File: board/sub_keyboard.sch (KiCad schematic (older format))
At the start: 48 parts

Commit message: Updated keyboard
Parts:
- removed D? (x23): D, symbol Device:D
- removed SW? (x23): SW_SPST, symbol Switch:SW_SPST
- added D802, D803, D804, D805, D806, D807, D808, D809, D810, D811, D812, D813, D814, D815, D816, D817, D818, D819, D820, D821, D822, D823, D824, D825, D826, D827, D828, D829, D830: D, symbol Device:D
- added SW802, SW803, SW804, SW805, SW806, SW807, SW808, SW809, SW810, SW811, SW812, SW813, SW814, SW815, SW816, SW817, SW818, SW819, SW820, SW821, SW822, SW823, SW824, SW825, SW826, SW827, SW828, SW829, SW830: SW_SPST, symbol Switch:SW_SPST
- gave numbers to parts that had none: 2
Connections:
- net labels added: column[0], column[1], column[2], column[3], column[4], column[5], row[0], row[1], row[2], row[3], row[4]
- wire segments 0 -> 120
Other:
- moved on the sheet: SW801

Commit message: More progress on the schematic. 6502 Done.
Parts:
- renumbered D801 to D701, D802 to D702, D803 to D703, D804 to D704, D805 to D705, D806 to D706, D807 to D707, D808 to D708, D809 to D709, D810 to D710, D811 to D711, D812 to D712, D813 to D713, D814 to D714, D815 to D715, D816 to D716, D817 to D717, D818 to D718, D819 to D719, D820 to D720, D821 to D721, D822 to D722, D823 to D723, D824 to D724, D825 to D725, D826 to D726, D827 to D727, D828 to D728, D829 to D729, D830 to D730, SW801 to SW701, SW802 to SW702, SW803 to SW703, SW804 to SW704, SW805 to SW705, SW806 to SW706, SW807 to SW707, SW808 to SW708, SW809 to SW709, SW810 to SW710, SW811 to SW711, SW812 to SW712, SW813 to SW713, SW814 to SW714, SW815 to SW715, SW816 to SW716, SW817 to SW717, SW818 to SW718, SW819 to SW719, SW820 to SW720, SW821 to SW721, SW822 to SW722, SW823 to SW723, SW824 to SW724, SW825 to SW725, SW826 to SW726, SW827 to SW727, SW828 to SW728, SW829 to SW729, SW830 to SW730

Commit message: Level converters complete, display almost done
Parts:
- removed D701, D702, D703, D704, D705, D706, D707, D708, D709, D710, D711, D712, D713, D714, D715, D716, D717, D718, D719, D720, D721, D722, D723, D724, D725, D726, D727, D728, D729, D730: D, symbol Device:D
- renumbered SW701 to SW1001, SW702 to SW1002, SW703 to SW1003, SW704 to SW1004, SW705 to SW1005, SW706 to SW1006, SW707 to SW1007, SW708 to SW1008, SW709 to SW1009, SW710 to SW1010, SW711 to SW1011, SW712 to SW1012, SW713 to SW1013, SW714 to SW1014, SW715 to SW1015, SW716 to SW1016, SW717 to SW1017, SW718 to SW1018, SW719 to SW1019, SW720 to SW1020, SW721 to SW1021, SW722 to SW1022, SW723 to SW1023, SW724 to SW1024, SW725 to SW1025, SW726 to SW1026, SW727 to SW1027, SW728 to SW1028, SW729 to SW1029, SW730 to SW1030

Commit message: More Schematic progress
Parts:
- renumbered SW1001 to SW901, SW1002 to SW902, SW1003 to SW903, SW1004 to SW904, SW1005 to SW905, SW1006 to SW906, SW1007 to SW907, SW1008 to SW908, SW1009 to SW909, SW1010 to SW910, SW1011 to SW911, SW1012 to SW912, SW1013 to SW913, SW1014 to SW914, SW1015 to SW915, SW1016 to SW916, SW1017 to SW917, SW1018 to SW918, SW1019 to SW919, SW1020 to SW920, SW1021 to SW921, SW1022 to SW922, SW1023 to SW923, SW1024 to SW924, SW1025 to SW925, SW1026 to SW926, SW1027 to SW927, SW1028 to SW928, SW1029 to SW929, SW1030 to SW930
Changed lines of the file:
@@
 $Descr A4 11693 8268
 encoding utf-8
-Sheet 10 15
+Sheet 9 14
 Title ""
 Date ""
@@
 row[4:0]
 $Comp
-L Switch:SW_SPST SW1001
+L Switch:SW_SPST SW901
 U 1 1 5A9DE7BF
 P 4600 2500
-F 0 "SW1001" H 4500 2450 50  0000 L CNN
+F 0 "SW901" H 4500 2450 50  0000 L CNN
 F 1 "SW_SPST" H 4450 2350 50  0001 L CNN
 F 2 "" H 4600 2500 50  0001 C CNN
@@
 $EndComp
 $Comp
-L Switch:SW_SPST SW1006
+L Switch:SW_SPST SW906
 U 1 1 5A9F6D51
 P 5250 2500
-F 0 "SW1006" H 5150 2450 50  0000 L CNN
+F 0 "SW906" H 5150 2450 50  0000 L CNN
 F 1 "SW_SPST" H 5100 2350 50  0001 L CNN
 F 2 "" H 5250 2500 50  0001 C CNN
@@
 $EndComp
 $Comp
-L Switch:SW_SPST SW1011
+L Switch:SW_SPST SW911
 U 1 1 5A9F724F
 P 5900 2500
-F 0 "SW1011" H 5800 2450 50  0000 L CNN
+F 0 "SW911" H 5800 2450 50  0000 L CNN
 F 1 "SW_SPST" H 5750 2350 50  0001 L CNN
 F 2 "" H 5900 2500 50  0001 C CNN
@@
 $EndComp
 $Comp
-L Switch:SW_SPST SW1016
+L Switch:SW_SPST SW916
 U 1 1 5A9F725B
 P 6550 2500
-F 0 "SW1016" H 6450 2450 50  0000 L CNN
+F 0 "SW916" H 6450 2450 50  0000 L CNN
 F 1 "SW_SPST" H 6400 2350 50  0001 L CNN
 F 2 "" H 6550 2500 50  0001 C CNN
@@
 $EndComp
 $Comp
-L Switch:SW_SPST SW1021
+L Switch:SW_SPST SW921
 U 1 1 5A9F738F
 P 7200 2500
-F 0 "SW1021" H 7100 2450 50  0000 L CNN
+F 0 "SW921" H 7100 2450 50  0000 L CNN
 F 1 "SW_SPST" H 7050 2350 50  0001 L CNN
 F 2 "" H 7200 2500 50  0001 C CNN
@@
 $EndComp
 $Comp
-L Switch:SW_SPST SW1026
+L Switch:SW_SPST SW926
 U 1 1 5A9F739B
 P 7850 2500
-F 0 "SW1026" H 7750 2450 50  0000 L CNN
+F 0 "SW926" H 7750 2450 50  0000 L CNN
 F 1 "SW_SPST" H 7700 2350 50  0001 L CNN
 F 2 "" H 7850 2500 50  0001 C CNN
@@
 $EndComp
 $Comp
-L Switch:SW_SPST SW1002
+L Switch:SW_SPST SW902
 U 1 1 5A9F7527
 P 4600 3050
-F 0 "SW1002" H 4500 3000 50  0000 L CNN
+F 0 "SW902" H 4500 3000 50  0000 L CNN
 F 1 "SW_SPST" H 4450 2900 50  0001 L CNN
 F 2 "" H 4600 3050 50  0001 C CNN
@@
 $EndComp
 $Comp
-L Switch:SW_SPST SW1007
+L Switch:SW_SPST SW907
 U 1 1 5A9F7533
 P 5250 3050
-F 0 "SW1007" H 5150 3000 50  0000 L CNN
+F 0 "SW907" H 5150 3000 50  0000 L CNN
 F 1 "SW_SPST" H 5100 2900 50  0001 L CNN
 F 2 "" H 5250 3050 50  0001 C CNN
@@
 $EndComp
 $Comp
-L Switch:SW_SPST SW1012
+L Switch:SW_SPST SW912
 U 1 1 5A9F753F
 P 5900 3050
-F 0 "SW1012" H 5800 3000 50  0000 L CNN
+F 0 "SW912" H 5800 3000 50  0000 L CNN
 F 1 "SW_SPST" H 5750 2900 50  0001 L CNN
 F 2 "" H 5900 3050 50  0001 C CNN
@@
 $EndComp
 $Comp
-L Switch:SW_SPST SW1017
+L Switch:SW_SPST SW917
 U 1 1 5A9F754B
 P 6550 3050
-F 0 "SW1017" H 6450 3000 50  0000 L CNN
+F 0 "SW917" H 6450 3000 50  0000 L CNN
 F 1 "SW_SPST" H 6400 2900 50  0001 L CNN
 F 2 "" H 6550 3050 50  0001 C CNN
@@
 $EndComp
 $Comp
-L Switch:SW_SPST SW1022
+L Switch:SW_SPST SW922
 U 1 1 5A9F7557
 P 7200 3050
-F 0 "SW1022" H 7100 3000 50  0000 L CNN
+F 0 "SW922" H 7100 3000 50  0000 L CNN
 F 1 "SW_SPST" H 7050 2900 50  0001 L CNN
 F 2 "" H 7200 3050 50  0001 C CNN
@@
 $EndComp
 $Comp
-L Switch:SW_SPST SW1027
+L Switch:SW_SPST SW927
 U 1 1 5A9F7563
 P 7850 3050
-F 0 "SW1027" H 7750 3000 50  0000 L CNN
+F 0 "SW927" H 7750 3000 50  0000 L CNN
 F 1 "SW_SPST" H 7700 2900 50  0001 L CNN
 F 2 "" H 7850 3050 50  0001 C CNN
@@
 $EndComp
 $Comp
-L Switch:SW_SPST SW1003
+L Switch:SW_SPST SW903
 U 1 1 5A9F8C97
 P 4600 3600
-F 0 "SW1003" H 4500 3550 50  0000 L CNN
+F 0 "SW903" H 4500 3550 50  0000 L CNN
 F 1 "SW_SPST" H 4450 3450 50  0001 L CNN
 F 2 "" H 4600 3600 50  0001 C CNN
@@
 $EndComp
 $Comp
-L Switch:SW_SPST SW1008
+L Switch:SW_SPST SW908
 U 1 1 5A9F8CA3
 P 5250 3600
-F 0 "SW1008" H 5150 3550 50  0000 L CNN
+F 0 "SW908" H 5150 3550 50  0000 L CNN
 F 1 "SW_SPST" H 5100 3450 50  0001 L CNN
 F 2 "" H 5250 3600 50  0001 C CNN
@@
 $EndComp
 $Comp
-L Switch:SW_SPST SW1013
+L Switch:SW_SPST SW913
 U 1 1 5A9F8CAF
 P 5900 3600
-F 0 "SW1013" H 5800 3550 50  0000 L CNN
+F 0 "SW913" H 5800 3550 50  0000 L CNN
 F 1 "SW_SPST" H 5750 3450 50  0001 L CNN
 F 2 "" H 5900 3600 50  0001 C CNN
@@
 $EndComp
 $Comp
-L Switch:SW_SPST SW1018
+L Switch:SW_SPST SW918
 U 1 1 5A9F8CBB
 P 6550 3600
-F 0 "SW1018" H 6450 3550 50  0000 L CNN
+F 0 "SW918" H 6450 3550 50  0000 L CNN
 F 1 "SW_SPST" H 6400 3450 50  0001 L CNN
 F 2 "" H 6550 3600 50  0001 C CNN
@@
 $EndComp
 $Comp
-L Switch:SW_SPST SW1023
+L Switch:SW_SPST SW923
 U 1 1 5A9F8CC7
 P 7200 3600
-F 0 "SW1023" H 7100 3550 50  0000 L CNN
+F 0 "SW923" H 7100 3550 50  0000 L CNN
 F 1 "SW_SPST" H 7050 3450 50  0001 L CNN
 F 2 "" H 7200 3600 50  0001 C CNN
@@
 $EndComp
 $Comp
-L Switch:SW_SPST SW1028
+L Switch:SW_SPST SW928
 U 1 1 5A9F8CD3
 P 7850 3600
-F 0 "SW1028" H 7750 3550 50  0000 L CNN
+F 0 "SW928" H 7750 3550 50  0000 L CNN
 F 1 "SW_SPST" H 7700 3450 50  0001 L CNN
 F 2 "" H 7850 3600 50  0001 C CNN
@@
 $EndComp
 $Comp
-L Switch:SW_SPST SW1004
+L Switch:SW_SPST SW904
 U 1 1 5A9F94D7
 P 4600 4150
-F 0 "SW1004" H 4500 4100 50  0000 L CNN
+F 0 "SW904" H 4500 4100 50  0000 L CNN
 F 1 "SW_SPST" H 4450 4000 50  0001 L CNN
 F 2 "" H 4600 4150 50  0001 C CNN
@@
 $EndComp
 $Comp
-L Switch:SW_SPST SW1009
+L Switch:SW_SPST SW909
 U 1 1 5A9F94E3
 P 5250 4150
-F 0 "SW1009" H 5150 4100 50  0000 L CNN
+F 0 "SW909" H 5150 4100 50  0000 L CNN
 F 1 "SW_SPST" H 5100 4000 50  0001 L CNN
 F 2 "" H 5250 4150 50  0001 C CNN
@@
 $EndComp
 $Comp
-L Switch:SW_SPST SW1014
+L Switch:SW_SPST SW914
 U 1 1 5A9F94EF
 P 5900 4150
-F 0 "SW1014" H 5800 4100 50  0000 L CNN
+F 0 "SW914" H 5800 4100 50  0000 L CNN
 F 1 "SW_SPST" H 5750 4000 50  0001 L CNN
 F 2 "" H 5900 4150 50  0001 C CNN
@@
 $EndComp
 $Comp
-L Switch:SW_SPST SW1019
+L Switch:SW_SPST SW919
 U 1 1 5A9F94FB
 P 6550 4150
-F 0 "SW1019" H 6450 4100 50  0000 L CNN
+F 0 "SW919" H 6450 4100 50  0000 L CNN
 F 1 "SW_SPST" H 6400 4000 50  0001 L CNN
 F 2 "" H 6550 4150 50  0001 C CNN
@@
 $EndComp
 $Comp
-L Switch:SW_SPST SW1024
+L Switch:SW_SPST SW924
 U 1 1 5A9F9507
 P 7200 4150
-F 0 "SW1024" H 7100 4100 50  0000 L CNN
+F 0 "SW924" H 7100 4100 50  0000 L CNN
 F 1 "SW_SPST" H 7050 4000 50  0001 L CNN
 F 2 "" H 7200 4150 50  0001 C CNN
@@
 $EndComp
 $Comp
-L Switch:SW_SPST SW1029
+L Switch:SW_SPST SW929
 U 1 1 5A9F9513
 P 7850 4150
-F 0 "SW1029" H 7750 4100 50  0000 L CNN
+F 0 "SW929" H 7750 4100 50  0000 L CNN
 F 1 "SW_SPST" H 7700 4000 50  0001 L CNN
 F 2 "" H 7850 4150 50  0001 C CNN
@@
 $EndComp
 $Comp
-L Switch:SW_SPST SW1005
+L Switch:SW_SPST SW905
 U 1 1 5A9F951F
 P 4600 4700
-F 0 "SW1005" H 4500 4650 50  0000 L CNN
+F 0 "SW905" H 4500 4650 50  0000 L CNN
 F 1 "SW_SPST" H 4450 4550 50  0001 L CNN
 F 2 "" H 4600 4700 50  0001 C CNN
@@
 $EndComp
 $Comp
-L Switch:SW_SPST SW1010
+L Switch:SW_SPST SW910
 U 1 1 5A9F952B
 P 5250 4700
-F 0 "SW1010" H 5150 4650 50  0000 L CNN
+F 0 "SW910" H 5150 4650 50  0000 L CNN
 F 1 "SW_SPST" H 5100 4550 50  0001 L CNN
 F 2 "" H 5250 4700 50  0001 C CNN
@@
 $EndComp
 $Comp
-L Switch:SW_SPST SW1015
+L Switch:SW_SPST SW915
 U 1 1 5A9F9537
 P 5900 4700
-F 0 "SW1015" H 5800 4650 50  0000 L CNN
+F 0 "SW915" H 5800 4650 50  0000 L CNN
 F 1 "SW_SPST" H 5750 4550 50  0001 L CNN
 F 2 "" H 5900 4700 50  0001 C CNN
@@
 $EndComp
 $Comp
-L Switch:SW_SPST SW1020
+L Switch:SW_SPST SW920
 U 1 1 5A9F9543
 P 6550 4700
-F 0 "SW1020" H 6450 4650 50  0000 L CNN
+F 0 "SW920" H 6450 4650 50  0000 L CNN
 F 1 "SW_SPST" H 6400 4550 50  0001 L CNN
 F 2 "" H 6550 4700 50  0001 C CNN
@@
 $EndComp
 $Comp
-L Switch:SW_SPST SW1025
+L Switch:SW_SPST SW925
 U 1 1 5A9F954F
 P 7200 4700
-F 0 "SW1025" H 7100 4650 50  0000 L CNN
+F 0 "SW925" H 7100 4650 50  0000 L CNN
 F 1 "SW_SPST" H 7050 4550 50  0001 L CNN
 F 2 "" H 7200 4700 50  0001 C CNN
@@
 $EndComp
 $Comp
-L Switch:SW_SPST SW1030
+L Switch:SW_SPST SW930
 U 1 1 5A9F955B
 P 7850 4700
-F 0 "SW1030" H 7750 4650 50  0000 L CNN
+F 0 "SW930" H 7750 4650 50  0000 L CNN
 F 1 "SW_SPST" H 7700 4550 50  0001 L CNN
 F 2 "" H 7850 4700 50  0001 C CNN

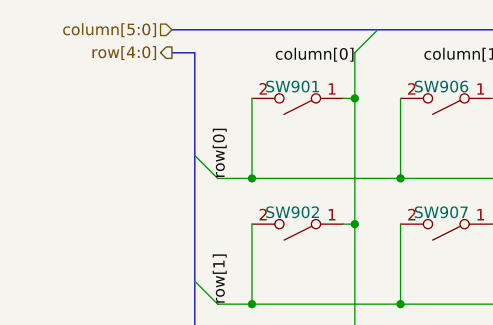
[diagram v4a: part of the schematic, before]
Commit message: Bus signal connectivity rebuilt
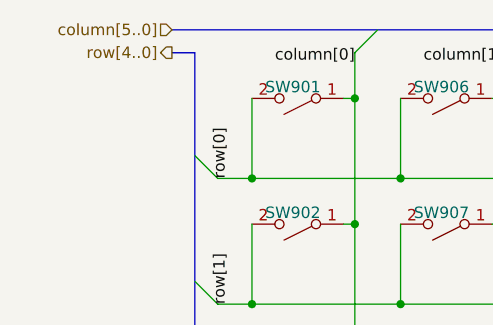
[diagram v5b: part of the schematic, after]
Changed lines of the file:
@@
 $EndDescr
 Text HLabel 4050 2200 0    50   Input ~ 0
-column[5:0]
+column[5..0]
 Text HLabel 4050 2300 0    50   Output ~ 0
-row[4:0]
+row[4..0]
 $Comp
 L Switch:SW_SPST SW901

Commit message: Schematics mostly complete
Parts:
- renumbered SW906 to SW902, SW911 to SW903, SW916 to SW904, SW921 to SW905, SW926 to SW906, SW902 to SW907, SW907 to SW908, SW912 to SW909, SW917 to SW910, SW922 to SW911, SW927 to SW912, SW903 to SW913, SW908 to SW914, SW913 to SW915, SW918 to SW916, SW923 to SW917, SW928 to SW918, SW904 to SW919, SW909 to SW920, SW914 to SW921, SW919 to SW922, SW924 to SW923, SW929 to SW924, SW905 to SW925, SW910 to SW926, SW915 to SW927, SW920 to SW928, SW925 to SW929
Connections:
- net column[0] renamed column0
- net column[1] renamed column1
- net column[2] renamed column2
- net column[3] renamed column3
- net column[4] renamed column4
- net column[5] renamed column5
- net row[0] renamed row0
- net row[1] renamed row1
- net row[2] renamed row2
- net row[3] renamed row3
- net row[4] renamed row4
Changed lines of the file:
@@
 $EndComp
 $Comp
-L Switch:SW_SPST SW906
+L Switch:SW_SPST SW902
 U 1 1 5A9F6D51
 P 5250 2500
-F 0 "SW906" H 5150 2450 50  0000 L CNN
+F 0 "SW902" H 5150 2450 50  0000 L CNN
 F 1 "SW_SPST" H 5100 2350 50  0001 L CNN
 F 2 "" H 5250 2500 50  0001 C CNN
@@
 $EndComp
 $Comp
-L Switch:SW_SPST SW911
+L Switch:SW_SPST SW903
 U 1 1 5A9F724F
 P 5900 2500
-F 0 "SW911" H 5800 2450 50  0000 L CNN
+F 0 "SW903" H 5800 2450 50  0000 L CNN
 F 1 "SW_SPST" H 5750 2350 50  0001 L CNN
 F 2 "" H 5900 2500 50  0001 C CNN
@@
 $EndComp
 $Comp
-L Switch:SW_SPST SW916
+L Switch:SW_SPST SW904
 U 1 1 5A9F725B
 P 6550 2500
-F 0 "SW916" H 6450 2450 50  0000 L CNN
+F 0 "SW904" H 6450 2450 50  0000 L CNN
 F 1 "SW_SPST" H 6400 2350 50  0001 L CNN
 F 2 "" H 6550 2500 50  0001 C CNN
@@
 $EndComp
 $Comp
-L Switch:SW_SPST SW921
+L Switch:SW_SPST SW905
 U 1 1 5A9F738F
 P 7200 2500
-F 0 "SW921" H 7100 2450 50  0000 L CNN
+F 0 "SW905" H 7100 2450 50  0000 L CNN
 F 1 "SW_SPST" H 7050 2350 50  0001 L CNN
 F 2 "" H 7200 2500 50  0001 C CNN
@@
 $EndComp
 $Comp
-L Switch:SW_SPST SW926
+L Switch:SW_SPST SW906
 U 1 1 5A9F739B
 P 7850 2500
-F 0 "SW926" H 7750 2450 50  0000 L CNN
+F 0 "SW906" H 7750 2450 50  0000 L CNN
 F 1 "SW_SPST" H 7700 2350 50  0001 L CNN
 F 2 "" H 7850 2500 50  0001 C CNN
@@
 $EndComp
 $Comp
-L Switch:SW_SPST SW902
+L Switch:SW_SPST SW907
 U 1 1 5A9F7527
 P 4600 3050
-F 0 "SW902" H 4500 3000 50  0000 L CNN
+F 0 "SW907" H 4500 3000 50  0000 L CNN
 F 1 "SW_SPST" H 4450 2900 50  0001 L CNN
 F 2 "" H 4600 3050 50  0001 C CNN
@@
 $EndComp
 $Comp
-L Switch:SW_SPST SW907
+L Switch:SW_SPST SW908
 U 1 1 5A9F7533
 P 5250 3050
-F 0 "SW907" H 5150 3000 50  0000 L CNN
+F 0 "SW908" H 5150 3000 50  0000 L CNN
 F 1 "SW_SPST" H 5100 2900 50  0001 L CNN
 F 2 "" H 5250 3050 50  0001 C CNN
@@
 $EndComp
 $Comp
-L Switch:SW_SPST SW912
+L Switch:SW_SPST SW909
 U 1 1 5A9F753F
 P 5900 3050
-F 0 "SW912" H 5800 3000 50  0000 L CNN
+F 0 "SW909" H 5800 3000 50  0000 L CNN
 F 1 "SW_SPST" H 5750 2900 50  0001 L CNN
 F 2 "" H 5900 3050 50  0001 C CNN
@@
 $EndComp
 $Comp
-L Switch:SW_SPST SW917
+L Switch:SW_SPST SW910
 U 1 1 5A9F754B
 P 6550 3050
-F 0 "SW917" H 6450 3000 50  0000 L CNN
+F 0 "SW910" H 6450 3000 50  0000 L CNN
 F 1 "SW_SPST" H 6400 2900 50  0001 L CNN
 F 2 "" H 6550 3050 50  0001 C CNN
@@
 $EndComp
 $Comp
-L Switch:SW_SPST SW922
+L Switch:SW_SPST SW911
 U 1 1 5A9F7557
 P 7200 3050
-F 0 "SW922" H 7100 3000 50  0000 L CNN
+F 0 "SW911" H 7100 3000 50  0000 L CNN
 F 1 "SW_SPST" H 7050 2900 50  0001 L CNN
 F 2 "" H 7200 3050 50  0001 C CNN
@@
 $EndComp
 $Comp
-L Switch:SW_SPST SW927
+L Switch:SW_SPST SW912
 U 1 1 5A9F7563
 P 7850 3050
-F 0 "SW927" H 7750 3000 50  0000 L CNN
+F 0 "SW912" H 7750 3000 50  0000 L CNN
 F 1 "SW_SPST" H 7700 2900 50  0001 L CNN
 F 2 "" H 7850 3050 50  0001 C CNN
@@
 $EndComp
 $Comp
-L Switch:SW_SPST SW903
+L Switch:SW_SPST SW913
 U 1 1 5A9F8C97
 P 4600 3600
-F 0 "SW903" H 4500 3550 50  0000 L CNN
+F 0 "SW913" H 4500 3550 50  0000 L CNN
 F 1 "SW_SPST" H 4450 3450 50  0001 L CNN
 F 2 "" H 4600 3600 50  0001 C CNN
@@
 $EndComp
 $Comp
-L Switch:SW_SPST SW908
+L Switch:SW_SPST SW914
 U 1 1 5A9F8CA3
 P 5250 3600
-F 0 "SW908" H 5150 3550 50  0000 L CNN
+F 0 "SW914" H 5150 3550 50  0000 L CNN
 F 1 "SW_SPST" H 5100 3450 50  0001 L CNN
 F 2 "" H 5250 3600 50  0001 C CNN
@@
 $EndComp
 $Comp
-L Switch:SW_SPST SW913
+L Switch:SW_SPST SW915
 U 1 1 5A9F8CAF
 P 5900 3600
-F 0 "SW913" H 5800 3550 50  0000 L CNN
+F 0 "SW915" H 5800 3550 50  0000 L CNN
 F 1 "SW_SPST" H 5750 3450 50  0001 L CNN
 F 2 "" H 5900 3600 50  0001 C CNN
@@
 $EndComp
 $Comp
-L Switch:SW_SPST SW918
+L Switch:SW_SPST SW916
 U 1 1 5A9F8CBB
 P 6550 3600
-F 0 "SW918" H 6450 3550 50  0000 L CNN
+F 0 "SW916" H 6450 3550 50  0000 L CNN
 F 1 "SW_SPST" H 6400 3450 50  0001 L CNN
 F 2 "" H 6550 3600 50  0001 C CNN
@@
 $EndComp
 $Comp
-L Switch:SW_SPST SW923
+L Switch:SW_SPST SW917
 U 1 1 5A9F8CC7
 P 7200 3600
-F 0 "SW923" H 7100 3550 50  0000 L CNN
+F 0 "SW917" H 7100 3550 50  0000 L CNN
 F 1 "SW_SPST" H 7050 3450 50  0001 L CNN
 F 2 "" H 7200 3600 50  0001 C CNN
@@
 $EndComp
 $Comp
-L Switch:SW_SPST SW928
+L Switch:SW_SPST SW918
 U 1 1 5A9F8CD3
 P 7850 3600
-F 0 "SW928" H 7750 3550 50  0000 L CNN
+F 0 "SW918" H 7750 3550 50  0000 L CNN
 F 1 "SW_SPST" H 7700 3450 50  0001 L CNN
 F 2 "" H 7850 3600 50  0001 C CNN
@@
 $EndComp
 $Comp
-L Switch:SW_SPST SW904
+L Switch:SW_SPST SW919
 U 1 1 5A9F94D7
 P 4600 4150
-F 0 "SW904" H 4500 4100 50  0000 L CNN
+F 0 "SW919" H 4500 4100 50  0000 L CNN
 F 1 "SW_SPST" H 4450 4000 50  0001 L CNN
 F 2 "" H 4600 4150 50  0001 C CNN
@@
 $EndComp
 $Comp
-L Switch:SW_SPST SW909
+L Switch:SW_SPST SW920
 U 1 1 5A9F94E3
 P 5250 4150
-F 0 "SW909" H 5150 4100 50  0000 L CNN
+F 0 "SW920" H 5150 4100 50  0000 L CNN
 F 1 "SW_SPST" H 5100 4000 50  0001 L CNN
 F 2 "" H 5250 4150 50  0001 C CNN
@@
 $EndComp
 $Comp
-L Switch:SW_SPST SW914
+L Switch:SW_SPST SW921
 U 1 1 5A9F94EF
 P 5900 4150
-F 0 "SW914" H 5800 4100 50  0000 L CNN
+F 0 "SW921" H 5800 4100 50  0000 L CNN
 F 1 "SW_SPST" H 5750 4000 50  0001 L CNN
 F 2 "" H 5900 4150 50  0001 C CNN
@@
 $EndComp
 $Comp
-L Switch:SW_SPST SW919
+L Switch:SW_SPST SW922
 U 1 1 5A9F94FB
 P 6550 4150
-F 0 "SW919" H 6450 4100 50  0000 L CNN
+F 0 "SW922" H 6450 4100 50  0000 L CNN
 F 1 "SW_SPST" H 6400 4000 50  0001 L CNN
 F 2 "" H 6550 4150 50  0001 C CNN
@@
 $EndComp
 $Comp
-L Switch:SW_SPST SW924
+L Switch:SW_SPST SW923
 U 1 1 5A9F9507
 P 7200 4150
-F 0 "SW924" H 7100 4100 50  0000 L CNN
+F 0 "SW923" H 7100 4100 50  0000 L CNN
 F 1 "SW_SPST" H 7050 4000 50  0001 L CNN
 F 2 "" H 7200 4150 50  0001 C CNN
@@
 $EndComp
 $Comp
-L Switch:SW_SPST SW929
+L Switch:SW_SPST SW924
 U 1 1 5A9F9513
 P 7850 4150
-F 0 "SW929" H 7750 4100 50  0000 L CNN
+F 0 "SW924" H 7750 4100 50  0000 L CNN
 F 1 "SW_SPST" H 7700 4000 50  0001 L CNN
 F 2 "" H 7850 4150 50  0001 C CNN
@@
 $EndComp
 $Comp
-L Switch:SW_SPST SW905
+L Switch:SW_SPST SW925
 U 1 1 5A9F951F
 P 4600 4700
-F 0 "SW905" H 4500 4650 50  0000 L CNN
+F 0 "SW925" H 4500 4650 50  0000 L CNN
 F 1 "SW_SPST" H 4450 4550 50  0001 L CNN
 F 2 "" H 4600 4700 50  0001 C CNN
@@
 $EndComp
 $Comp
-L Switch:SW_SPST SW910
+L Switch:SW_SPST SW926
 U 1 1 5A9F952B
 P 5250 4700
-F 0 "SW910" H 5150 4650 50  0000 L CNN
+F 0 "SW926" H 5150 4650 50  0000 L CNN
 F 1 "SW_SPST" H 5100 4550 50  0001 L CNN
 F 2 "" H 5250 4700 50  0001 C CNN
@@
 $EndComp
 $Comp
-L Switch:SW_SPST SW915
+L Switch:SW_SPST SW927
 U 1 1 5A9F9537
 P 5900 4700
-F 0 "SW915" H 5800 4650 50  0000 L CNN
+F 0 "SW927" H 5800 4650 50  0000 L CNN
 F 1 "SW_SPST" H 5750 4550 50  0001 L CNN
 F 2 "" H 5900 4700 50  0001 C CNN
@@
 $EndComp
 $Comp
-L Switch:SW_SPST SW920
+L Switch:SW_SPST SW928
 U 1 1 5A9F9543
 P 6550 4700
-F 0 "SW920" H 6450 4650 50  0000 L CNN
+F 0 "SW928" H 6450 4650 50  0000 L CNN
 F 1 "SW_SPST" H 6400 4550 50  0001 L CNN
 F 2 "" H 6550 4700 50  0001 C CNN
@@
 $EndComp
 $Comp
-L Switch:SW_SPST SW925
+L Switch:SW_SPST SW929
 U 1 1 5A9F954F
 P 7200 4700
-F 0 "SW925" H 7100 4650 50  0000 L CNN
+F 0 "SW929" H 7100 4650 50  0000 L CNN
 F 1 "SW_SPST" H 7050 4550 50  0001 L CNN
 F 2 "" H 7200 4700 50  0001 C CNN
@@
 	8100 2300 8200 2200
 Text Label 4850 2350 2    50   ~ 0
-column[0]
+column0
 Text Label 5500 2350 2    50   ~ 0
-column[1]
+column1
 Text Label 6150 2350 2    50   ~ 0
-column[2]
+column2
 Text Label 6800 2350 2    50   ~ 0
-column[3]
+column3
 Text Label 7450 2350 2    50   ~ 0
-column[4]
+column4
 Text Label 8100 2350 2    50   ~ 0
-column[5]
+column5
 Entry Wire Line
 	4150 2750 4250 2850
@@
 	4150 2300 4050 2300
 Text Label 4300 2850 1    50   ~ 0
-row[0]
+row0
 Text Label 4300 3400 1    50   ~ 0
-row[1]
+row1
 Text Label 4300 3950 1    50   ~ 0
-row[2]
+row2
 Text Label 4300 4500 1    50   ~ 0
-row[3]
+row3
 Text Label 4300 5050 1    50   ~ 0
-row[4]
+row4
 Wire Wire Line
 	7650 2500 7650 2850
